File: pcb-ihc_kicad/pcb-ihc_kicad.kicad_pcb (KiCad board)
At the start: 2 copper layers, 100 x 160 mm, 69 parts, among them J1 D-IN with pullup, J10 D-IN with pulldown, J2 Screw_Terminal_01x01, J3 Screw_Terminal_01x01, J4 Screw_Terminal_01x01, J5 Screw_Terminal_01x01, J6 Screw_Terminal_01x01, J7 Screw_Terminal_01x01, J8 Screw_Terminal_01x01, J9 Screw_Terminal_01x01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

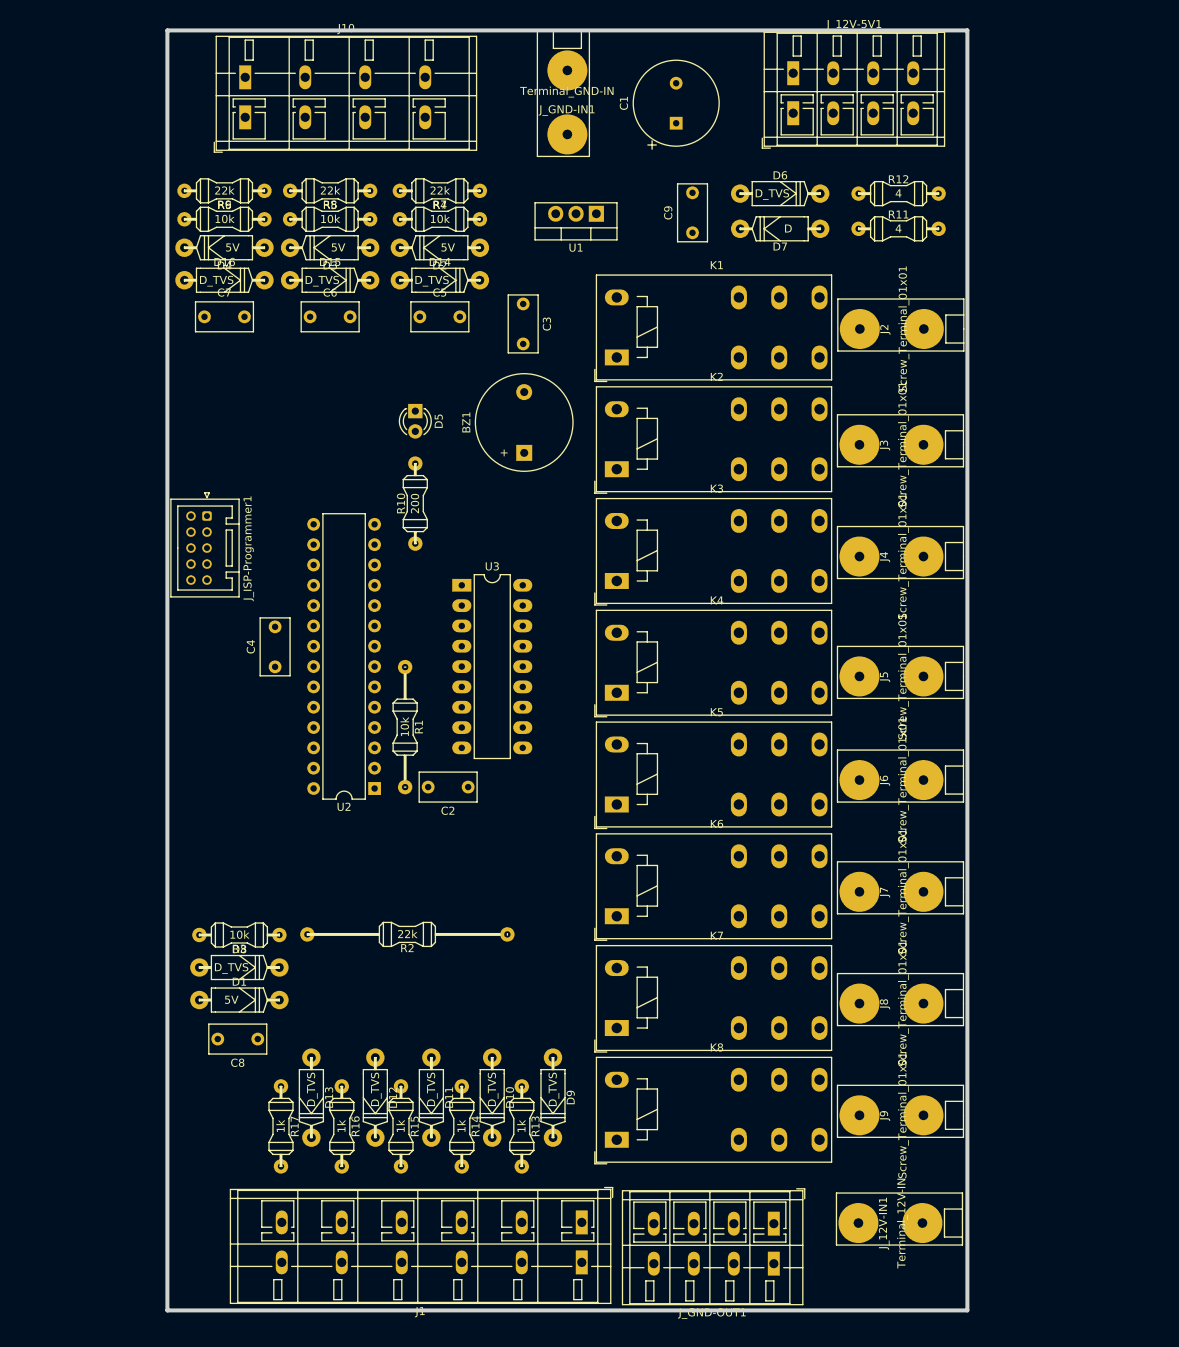
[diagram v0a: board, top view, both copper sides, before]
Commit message: Add 2x Mosfet, Change labels, Change layout
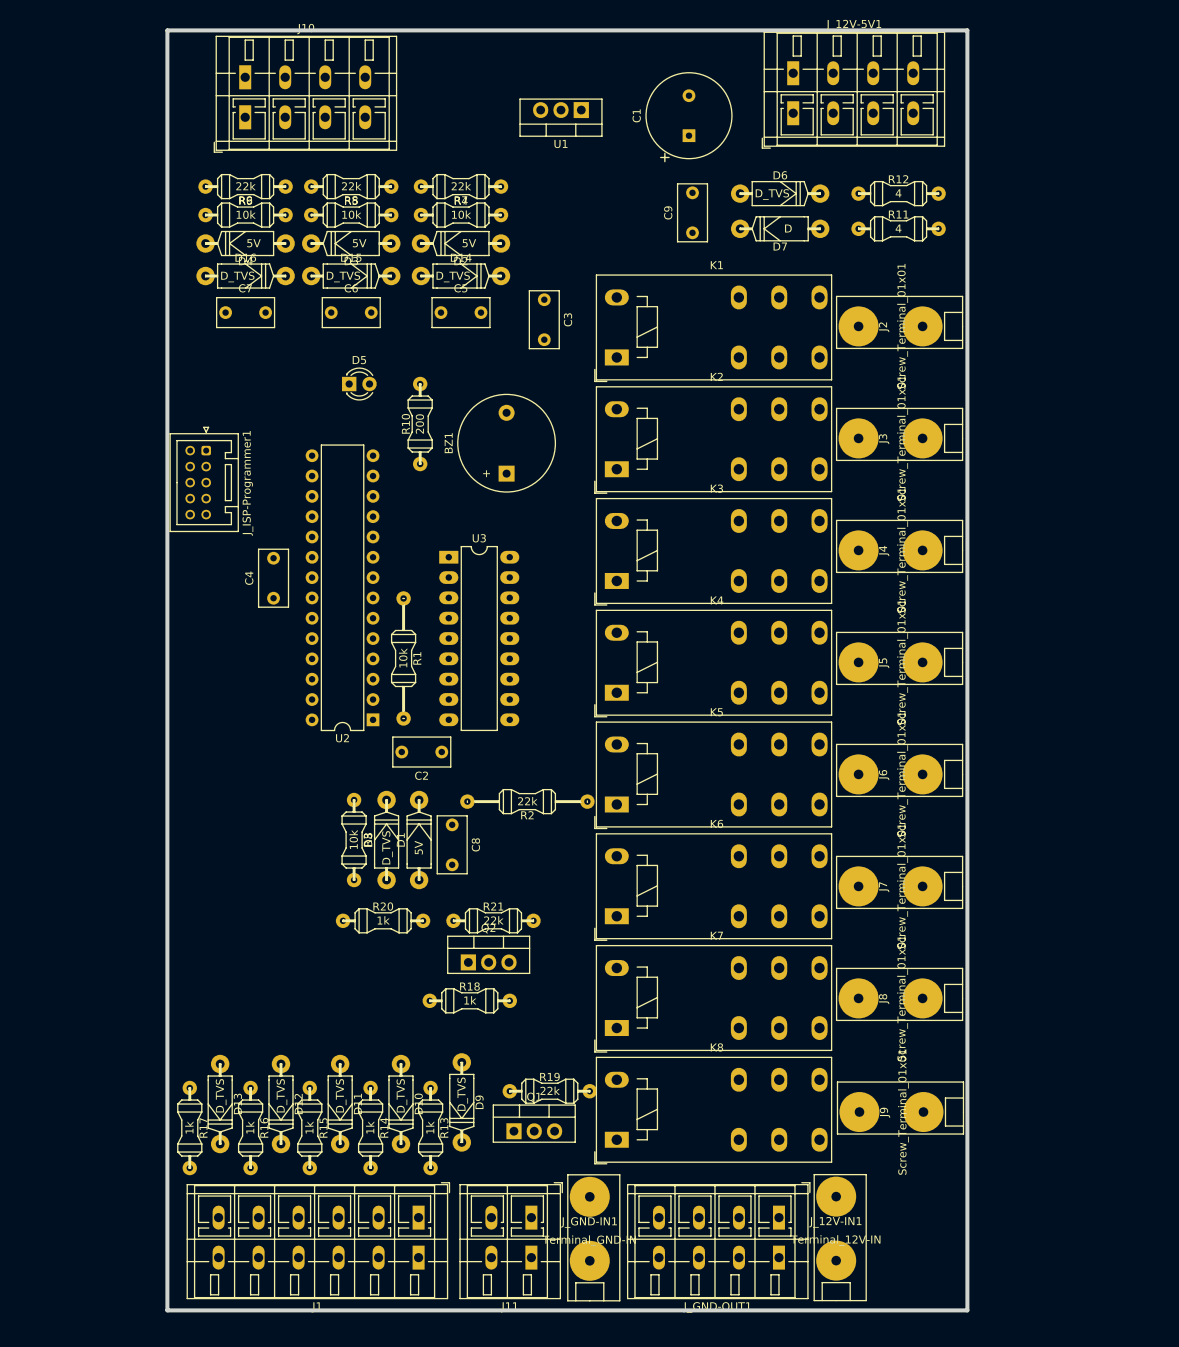
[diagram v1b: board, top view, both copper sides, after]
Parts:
- added J11: 2x N-Mosfet, TerminalBlock_WAGO:TerminalBlock_WAGO_236-402_1x02_P5.00mm_45Degree, F.Cu at (110.5, 168.4)
- added Q1: IRFZ24N, Package_TO_SOT_THT:TO-220-3_Vertical, F.Cu at (108.3, 152.6)
- added Q2: IRFZ24N, Package_TO_SOT_THT:TO-220-3_Vertical, F.Cu at (102.6, 131.5)
- added R18: 1k, custom_footprints:my_R10, F.Cu at (102.8, 136.3)
- added R19: 22k, custom_footprints:my_R10, F.Cu at (112.8, 147.6)
- added R20: 1k, custom_footprints:my_R10, F.Cu at (92.0, 126.3)
- added R21: 22k, custom_footprints:my_R10, F.Cu at (105.8, 126.3)
- J1: footprint TerminalBlock_WAGO:TerminalBlock_WAGO_236-506_1x06_P7.50mm_45Degree -> TerminalBlock_WAGO:TerminalBlock_WAGO_236-406_1x06_P5.00mm_45Degree
- J10: footprint TerminalBlock_WAGO:TerminalBlock_WAGO_236-504_1x04_P7.50mm_45Degree -> TerminalBlock_WAGO:TerminalBlock_WAGO_236-404_1x04_P5.00mm_45Degree
- R2: footprint custom_footprints:my_R25-long -> custom_footprints:my_R15-long
- moved J_GND-IN1 148.8 mm to (117.8, 168.8), turned to 180 degrees
- moved C8 36.2 mm to (100.6, 114.3), turned to -90 degrees
- moved D1 30.1 mm to (96.5, 116.2), turned to 90 degrees
- moved D8 24.3 mm to (92.4, 116.2), turned to 90 degrees
- moved R2 22.4 mm to (110.0, 111.4)
- moved J1 20.4 mm to (96.4, 168.4)
- moved R3 18.6 mm to (88.3, 116.2), turned to -90 degrees
- moved U1 13.1 mm to (116.7, 25.0)
- moved D12 11.8 mm to (79.2, 149.2)
- moved J_12V-IN1 11.8 mm to (148.6, 168.8), turned to 180 degrees
- moved D11 11.4 mm to (86.6, 149.2)
- moved D13 11.4 mm to (71.6, 149.2)
- moved D10 11.4 mm to (94.2, 149.2)
- moved D9 11.4 mm to (101.8, 149.0)
- moved R15 11.4 mm to (82.8, 152.2)
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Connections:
- net /PB6 (buzzer) renamed /buzzer
- net /PB6 - (ULN-I3) renamed /ULN-I3
- net /PB7 (led) renamed /led
- net /PB7 - (ULN-I2) renamed /ULN-I2
- net /PC1 (in pulldown) renamed /IN pulldown 1
- net /PC2 (in pulldown) renamed /IN pulldown 2
- net /PC3 (in pulldown) renamed /IN pulldown 3
- net /PD0 - (ULN-I8) renamed /ULN-I8
- net /PD1 - (ULN-I7) renamed /ULN-I7
- net /PD2 - (ULN-I6) renamed /ULN-I6
- net /PD3 - (ULN-I5) renamed /ULN-I5
- net /PD4 - (ULN-I4) renamed /ULN-I4
- net /PD7 - (ULN-I1) renamed /ULN-I1
- C8 pad 1: /PC0 (analog in U_supply) -> /Analog U_supply
- D1 pad 1: /PC0 (analog in U_supply) -> /Analog U_supply
- D10 pad 2: /PC5 (in) -> /IN pullup 4
- D11 pad 2: /PB0 (in) -> /IN pullup 3
- D12 pad 2: /PB1 (in) -> /IN pullup 2
- D13 pad 2: /PB2 (in) -> /PB3 (MOSI)
- D8 pad 1: /PC0 (analog in U_supply) -> /Analog U_supply
- D9 pad 2: /PC4 (in) -> /IN pullup 5
- J_12V-5V1 pad 1: +12V -> +5V
- J_12V-5V1 pad 2: +12V -> +5V
- J_12V-5V1 pad 3: +5V -> +12V
- J_12V-5V1 pad 4: +5V -> +12V
- J_ISP-Programmer1 pad 9: /PB4 (MISO) -> /IN pullup 2
- K8 pad 11: unconnected-(K8-Pad11) -> +12V
- R13 pad 1: /PC4 (in) -> /IN pullup 5
- R14 pad 1: /PC5 (in) -> /IN pullup 4
- R15 pad 1: /PB0 (in) -> /IN pullup 3
- R16 pad 1: /PB1 (in) -> /IN pullup 2
- R17 pad 1: /PB2 (in) -> /PB3 (MOSI)
- R2 pad 2: /PC0 (analog in U_supply) -> /Analog U_supply
- R3 pad 1: /PC0 (analog in U_supply) -> /Analog U_supply
- U2 pad 18: /PB4 (MISO) -> /IN pullup 2
- U2 pad 23: /PC0 (analog in U_supply) -> /IN pullup 3
- U2 pad 24: /PB2 (in) -> /IN pullup 4
- U2 pad 25: /PB1 (in) -> /IN pullup 5
- U2 pad 26: /PB0 (in) -> /Mosfet 1
- U2 pad 27: /PC5 (in) -> /Mosfet 2
- U2 pad 28: /PC4 (in) -> /Analog U_supply

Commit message: Optimize layout
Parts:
- J_ISP-Programmer1: footprint Connector_JST:JST_PUD_B10B-PUDSS_2x05_P2.00mm_Vertical -> custom_footprints:my_wannenstecker_2x5
- moved C3 21.2 mm to (107.7, 27.9), turned to 0 degrees
- moved C9 15.9 mm to (120.6, 27.9), turned to 180 degrees
- moved U1 4.51 mm to (114.0, 21.3)
- moved R19 4.09 mm to (112.8, 143.5)
- moved BZ1 2.78 mm to (106.9, 73.1)
- moved D14 1.77 mm to (103.1, 46.8)
- moved D2 1.77 mm to (103.1, 42.7)
- moved D5 1.62 mm to (86.1, 59.2)
- moved C5 1.58 mm to (100.4, 51.3)
- moved R4 1.53 mm to (103.1, 38.6)
- moved R7 1.42 mm to (103.1, 34.5)
- moved R21 1.38 mm to (104.6, 125.5)
- moved D15 1.38 mm to (88.9, 46.7)
- moved D3 1.38 mm to (88.9, 42.7)
- moved C6 1.23 mm to (86.1, 51.3)
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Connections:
- net /PB3 (MOSI) renamed /IN pullup 1

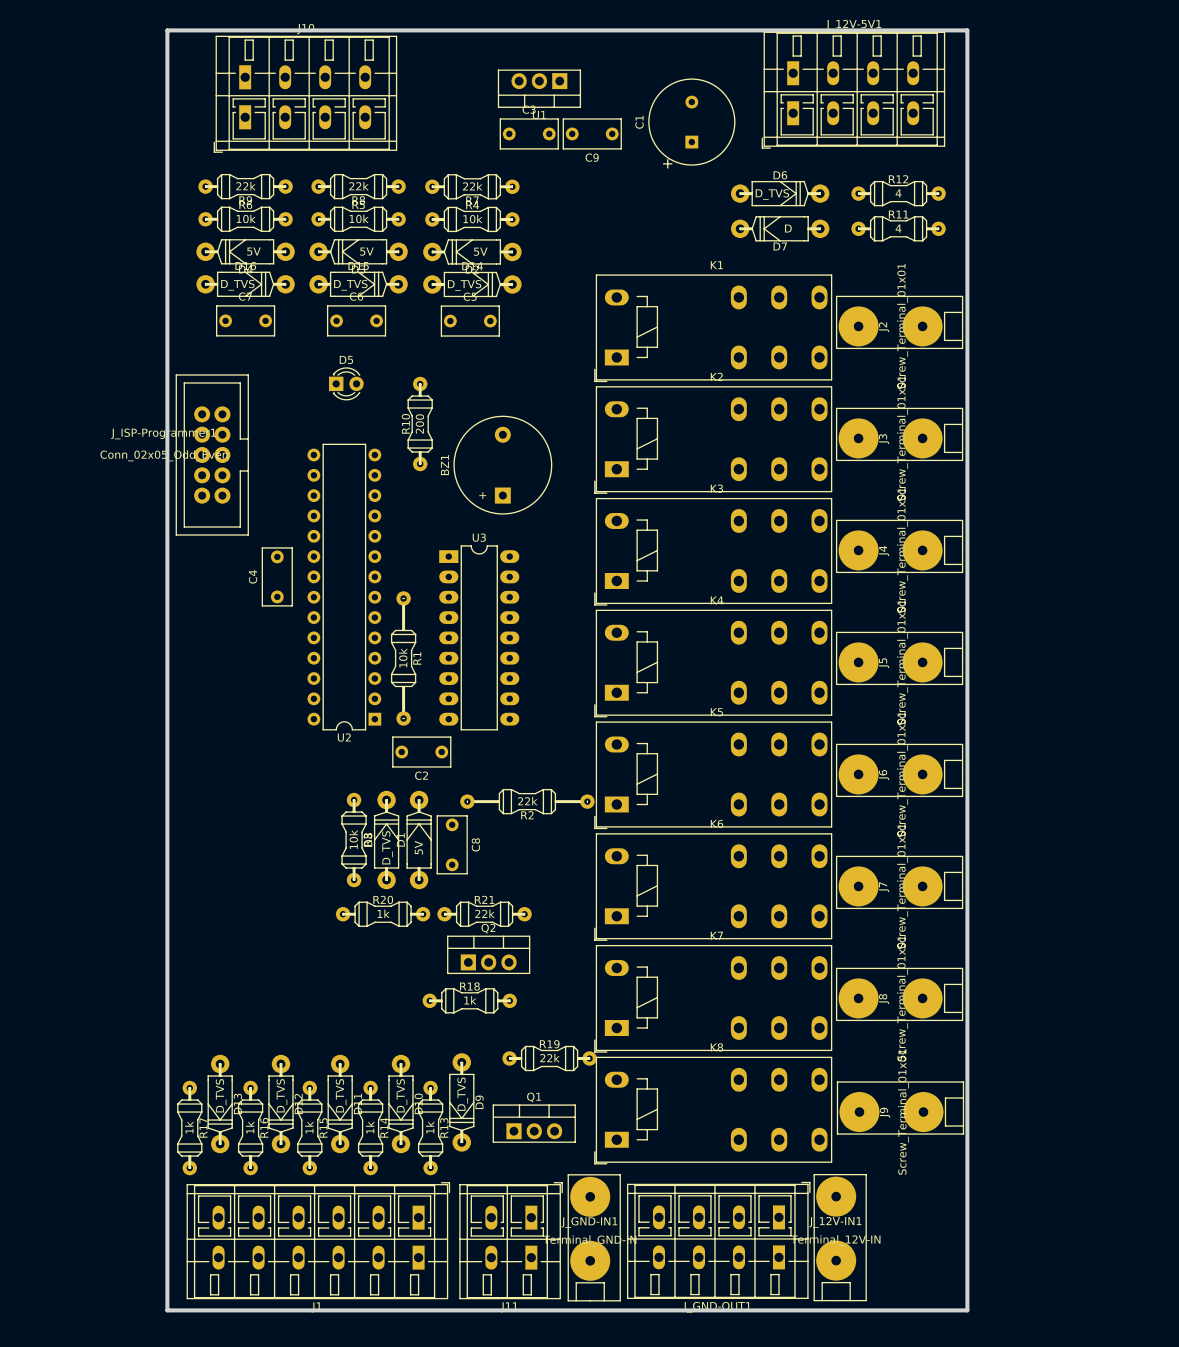
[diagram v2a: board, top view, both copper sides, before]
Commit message: Routing first version ready for validation
in this commit the entire routing of tracks was done. next step
validation and optimizations.
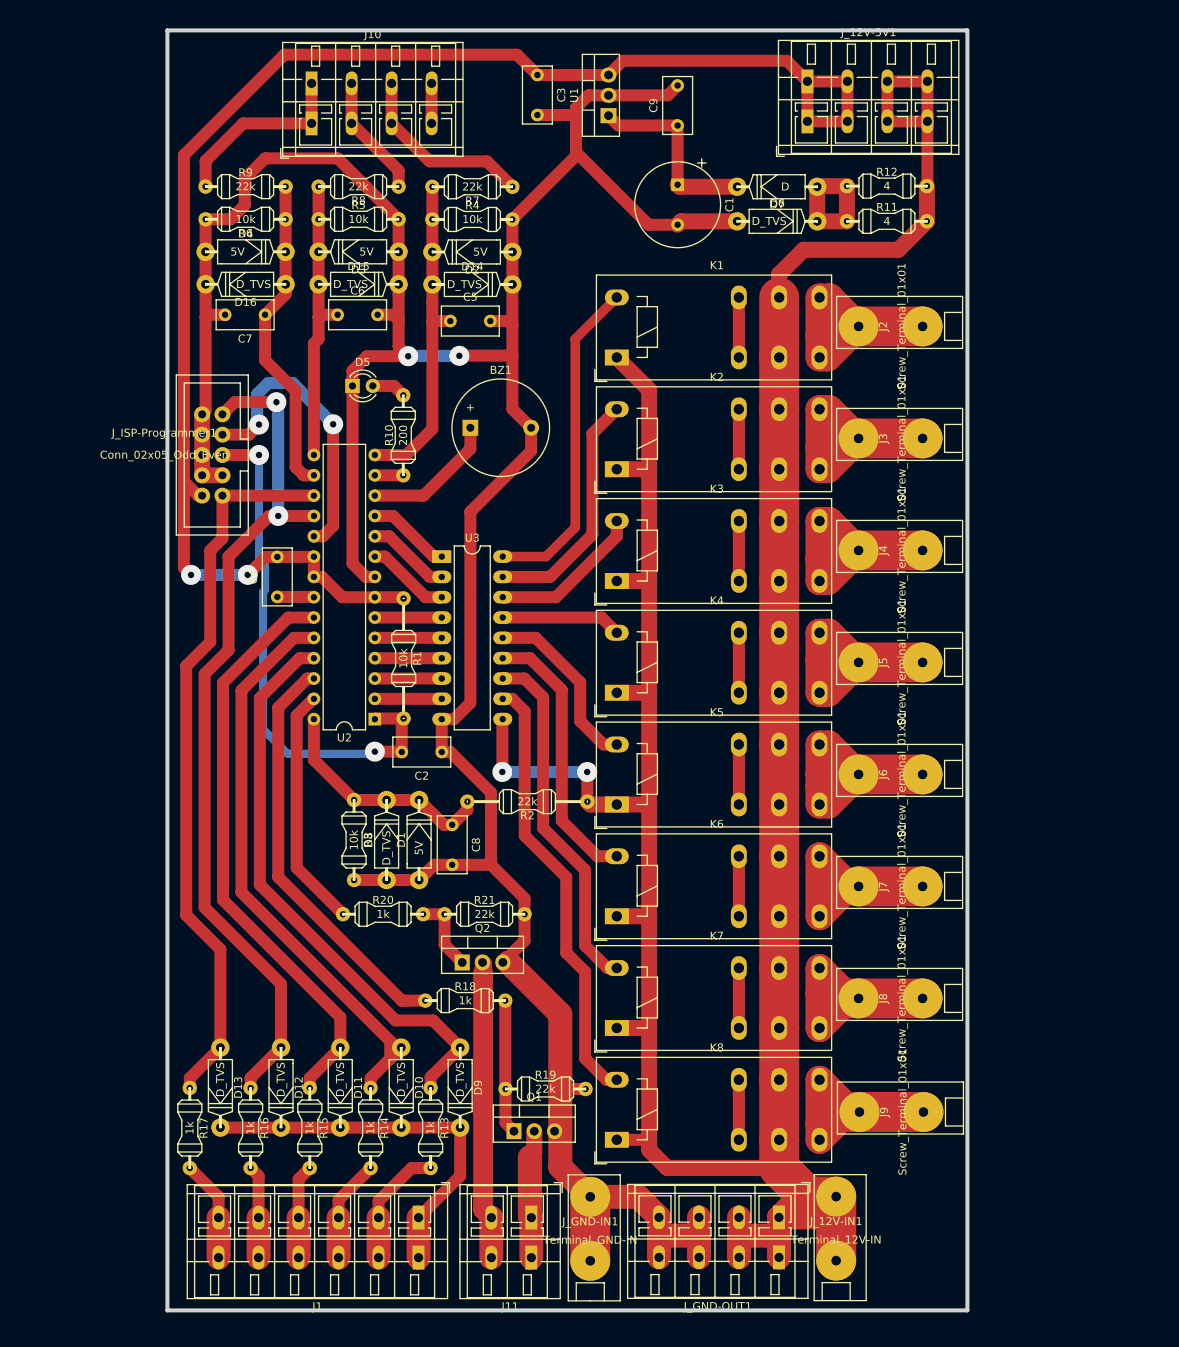
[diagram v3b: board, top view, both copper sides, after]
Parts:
- moved BZ1 9.40 mm to (102.9, 64.7), turned to 0 degrees
- moved J10 8.34 mm to (83.0, 21.6)
- moved C9 8.24 mm to (128.8, 26.9), turned to 90 degrees
- moved C3 8.16 mm to (111.3, 20.6), turned to -90 degrees
- moved U1 7.47 mm to (120.1, 25.7), turned to 90 degrees
- moved C1 5.62 mm to (128.8, 34.3), turned to -90 degrees
- moved D7 5.27 mm to (141.2, 34.5)
- moved C7 5.00 mm to (77.2, 50.5), turned to 180 degrees
- moved R19 3.84 mm to (112.3, 147.3)
- moved D6 3.48 mm to (141.2, 38.9)
- moved R10 2.54 mm to (94.5, 65.6)
- moved D10 2.05 mm to (94.2, 147.1)
- moved D13 2.05 mm to (71.6, 147.1)
- moved D11 2.05 mm to (86.6, 147.1)
- moved D12 2.05 mm to (79.2, 147.1)
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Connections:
- J10 pad 4: +12V -> unconnected-(J10-Pad4)
- J_GND-OUT1 pad 1: GND -> +12V
- J_GND-OUT1 pad 2: GND -> +12V
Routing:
- net GND: track 0.00 -> 447.6 mm, vias 0 -> 2
- net +12V: track 0.00 -> 382.4 mm, vias 0 -> 2
- net +5V: track 0.00 -> 193.0 mm, vias 0 -> 2
- net /IN pullup 2: track 0.00 -> 107.7 mm, vias 0 -> 2
- net /IN pullup 1: track 0.00 -> 90.7 mm
- net /IN pullup 4: track 0.00 -> 74.0 mm
- net /IN pullup 3: track 0.00 -> 73.0 mm
- net /IN pullup 5: track 0.00 -> 72.2 mm
- net /PC6 Reset: track 0.00 -> 65.9 mm, vias 0 -> 2
- net Net-(K8-PadA2): track 0.00 -> 55.0 mm
- net /Mosfet 1: track 0.00 -> 52.0 mm
- net Net-(K7-PadA2): track 0.00 -> 44.4 mm
- net Net-(K1-PadA2): track 0.00 -> 41.5 mm
- net /IN pulldown 1: track 0.00 -> 41.1 mm
- net /IN pulldown 3: track 0.00 -> 40.4 mm
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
